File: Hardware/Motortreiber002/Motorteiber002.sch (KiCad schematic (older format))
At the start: 0 parts

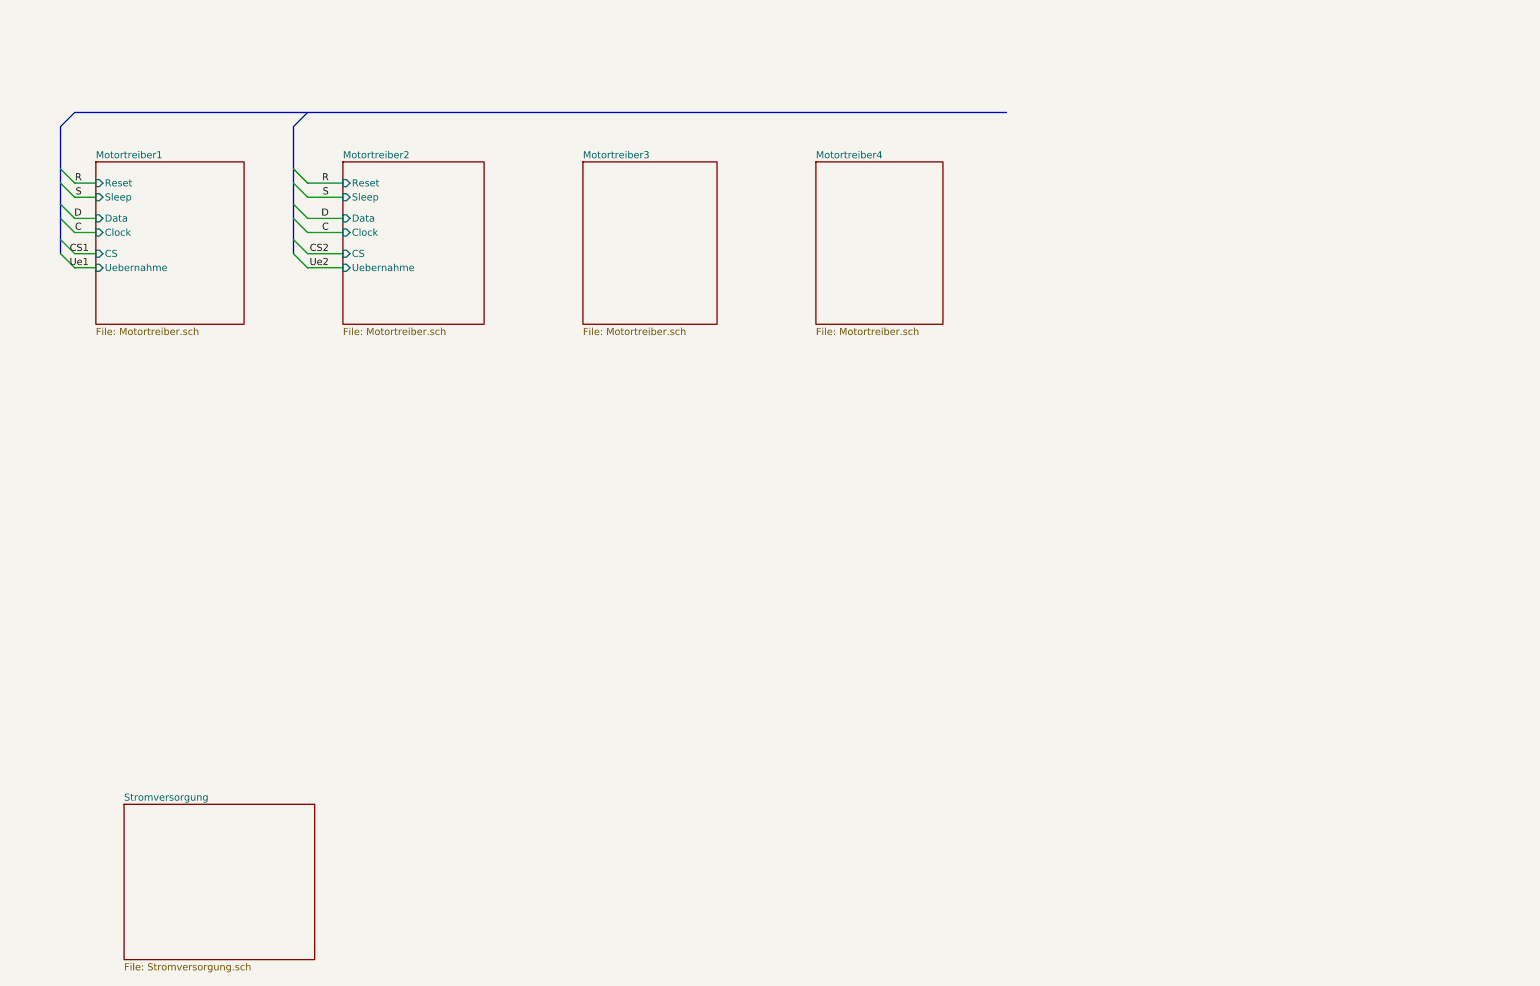
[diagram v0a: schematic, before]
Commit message: Mega64 hinzu
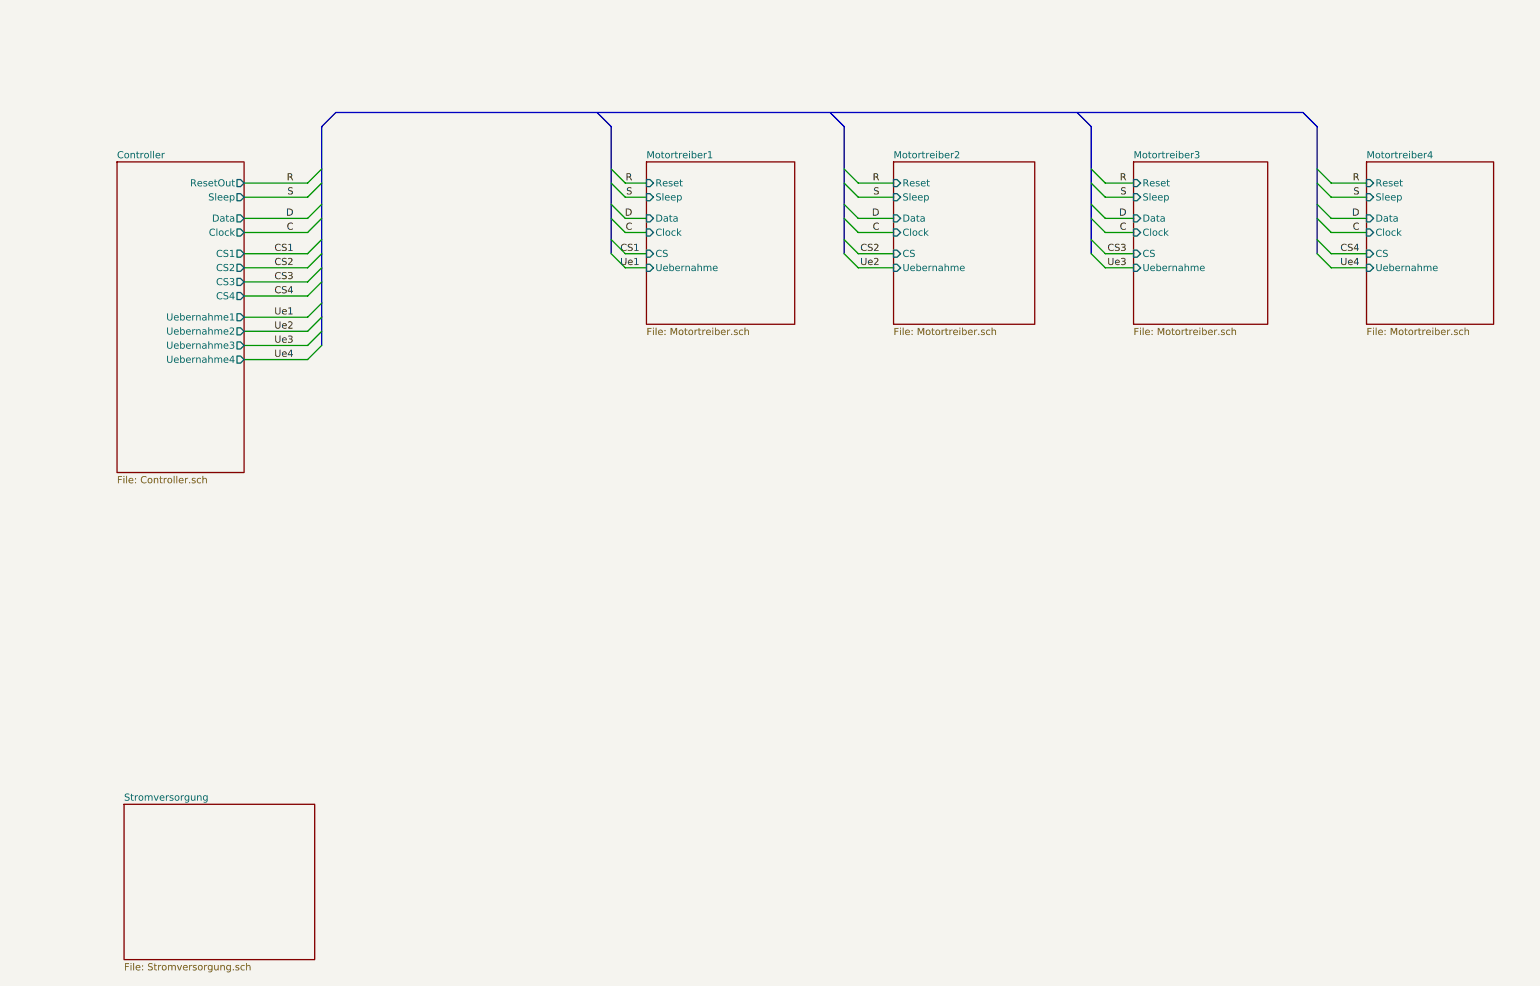
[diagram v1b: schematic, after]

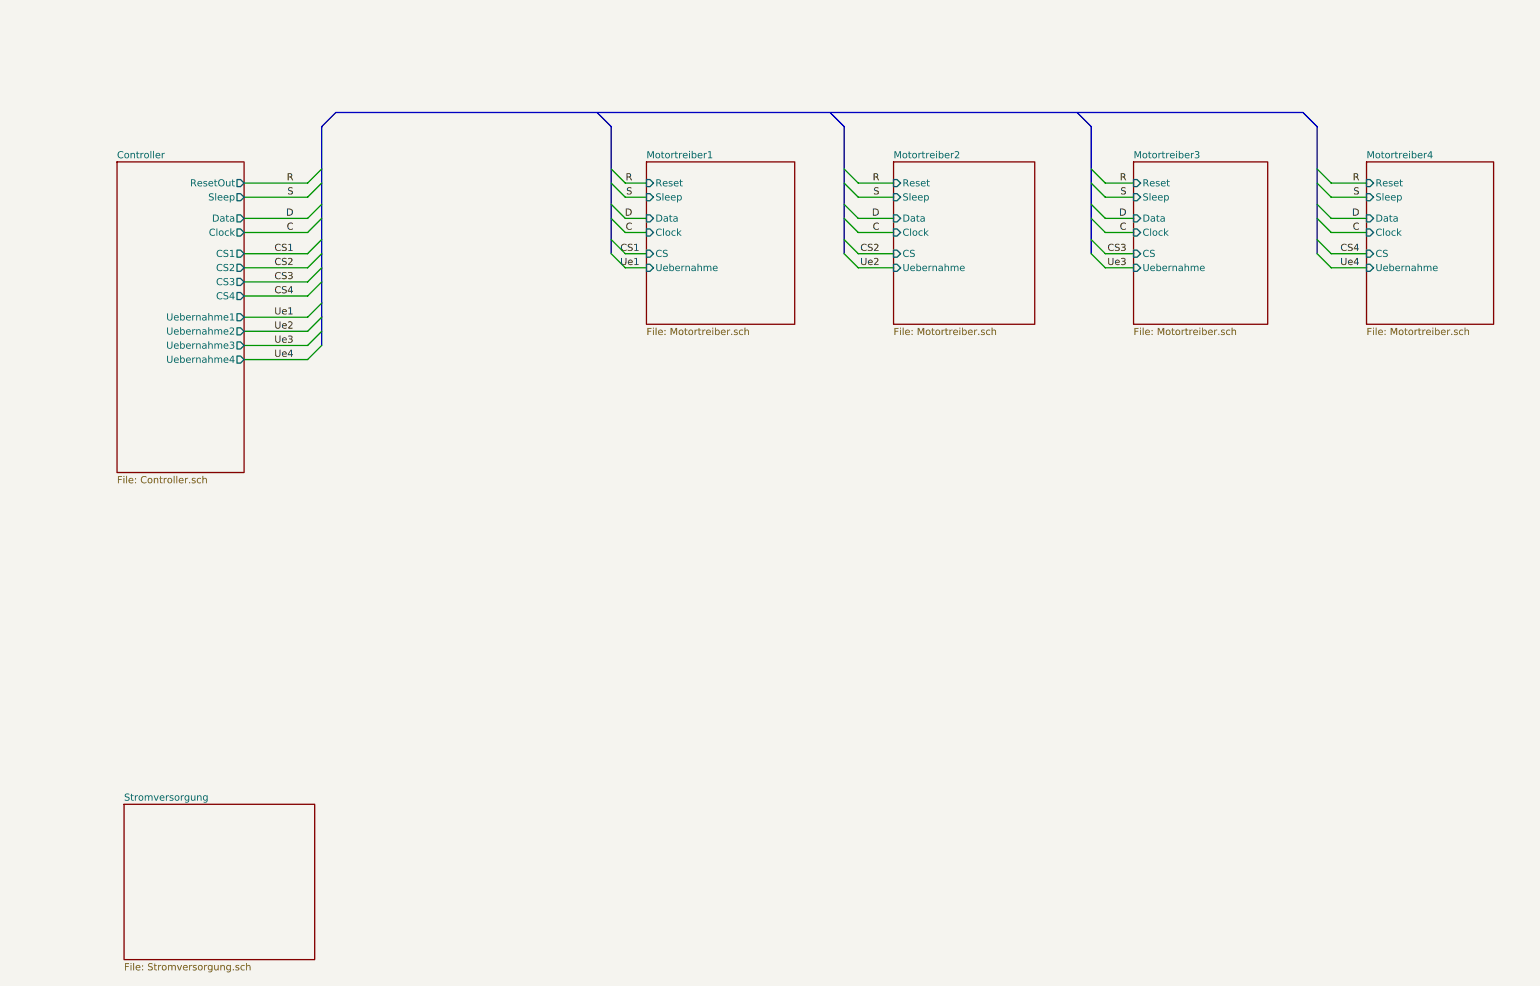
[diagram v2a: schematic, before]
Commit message: 16 Motortreiber 1 ATXMega 128 mit USB USB Anschluss noch nicht fertig
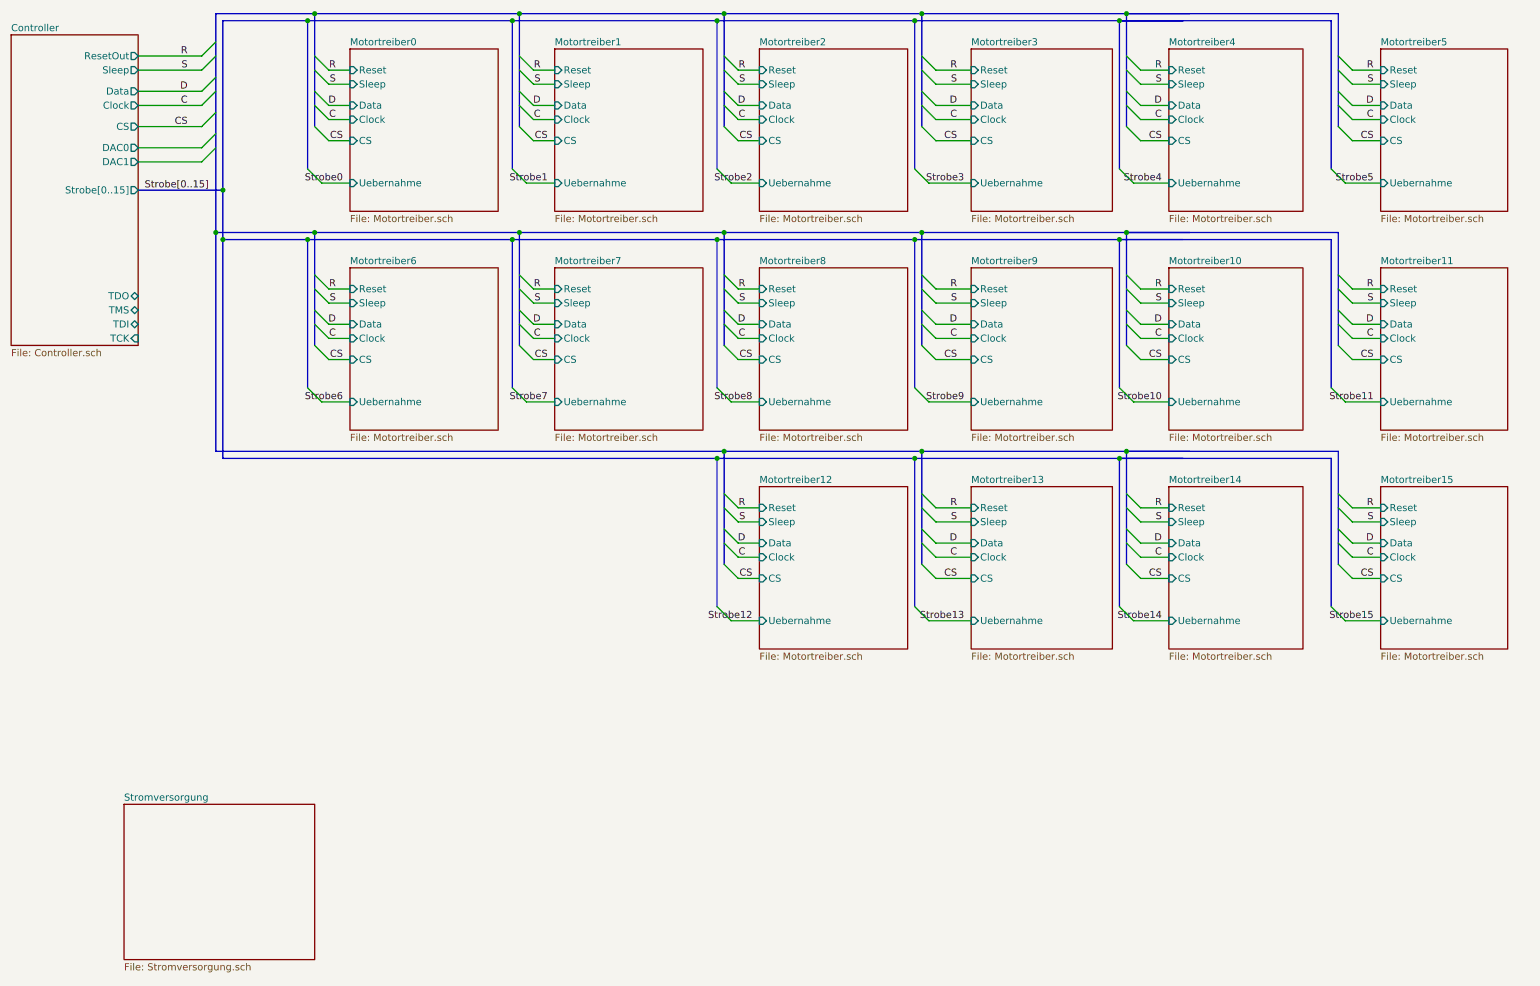
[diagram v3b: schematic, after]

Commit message: Annotation auf Seiten bezogen
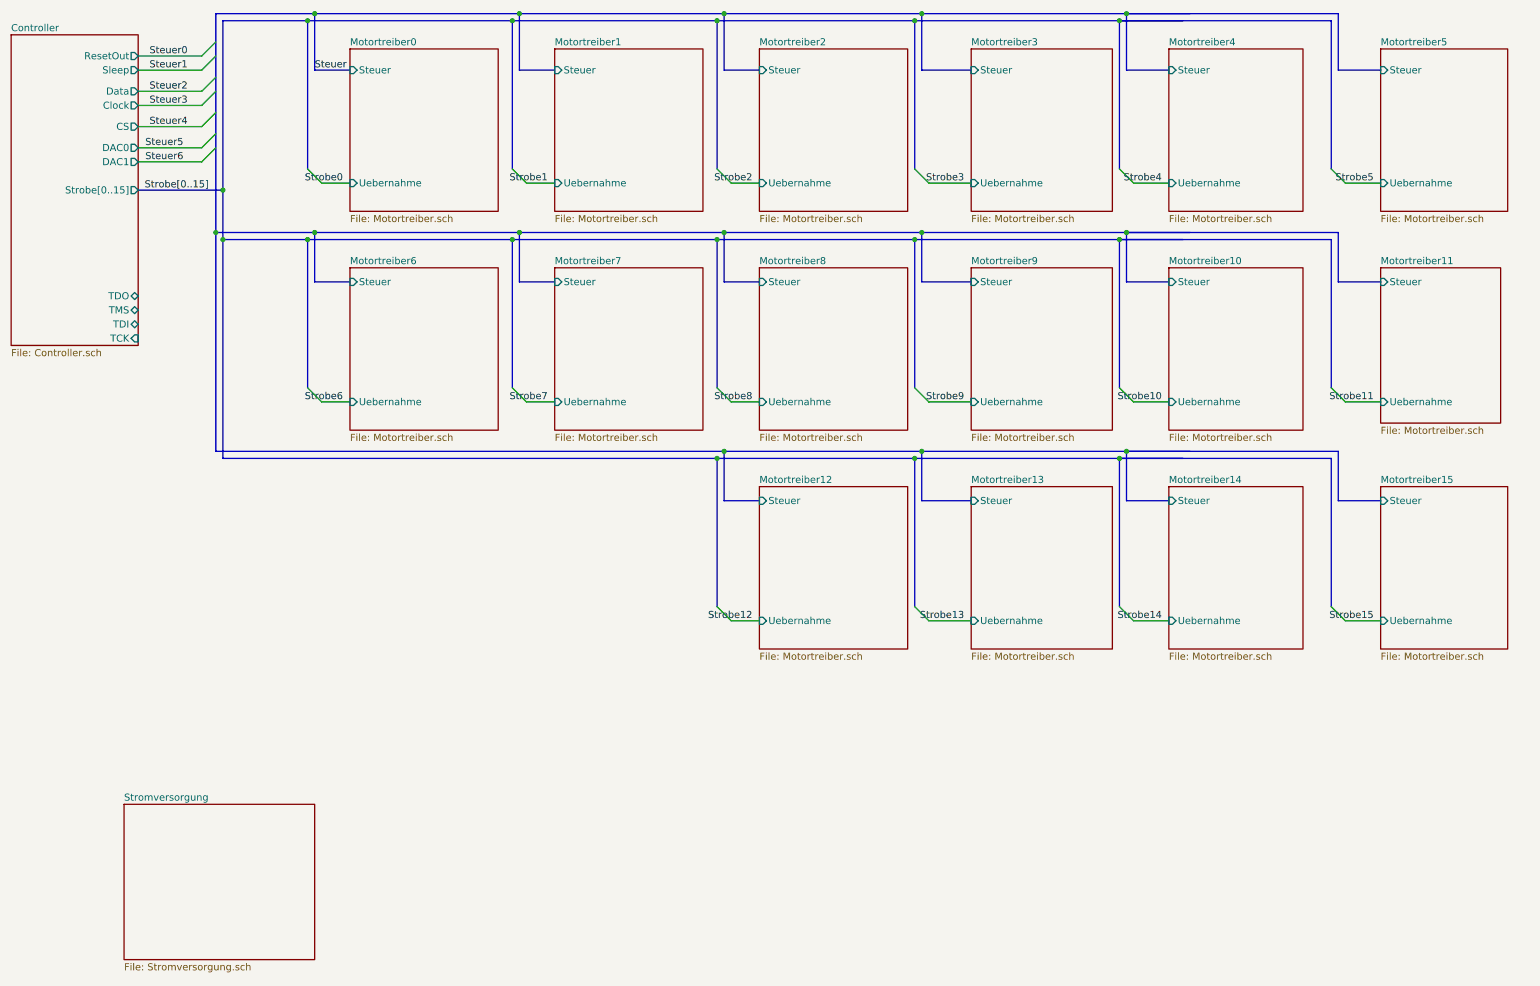
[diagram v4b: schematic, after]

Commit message: 16 Motortreiber
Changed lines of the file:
@@
 F1 "Motortreiber.sch" 50
 F2 "Uebernahme" I L 10300 1700 50
-F3 "Steuer" I L 10300 900 50
+F3 "Steuer[0..6]" I L 10300 900 50
 $EndSheet
 $Sheet
@@
 F1 "Motortreiber.sch" 50
 F2 "Uebernahme" I L 7400 1700 50
-F3 "Steuer" I L 7400 900 50
+F3 "Steuer[0..6]" I L 7400 900 50
 $EndSheet
 $Sheet
@@
 F1 "Motortreiber.sch" 50
 F2 "Uebernahme" I L 4450 1700 50
-F3 "Steuer" I L 4450 900 50
+F3 "Steuer[0..6]" I L 4450 900 50
 $EndSheet
 Wire Bus Line
@@
 F1 "Motortreiber.sch" 50
 F2 "Uebernahme" I L 3000 1700 50
-F3 "Steuer" I L 3000 900 50
+F3 "Steuer[0..6]" I L 3000 900 50
 $EndSheet
 Wire Bus Line
@@
 F1 "Motortreiber.sch" 50
 F2 "Uebernahme" I L 7400 3250 50
-F3 "Steuer" I L 7400 2400 50
+F3 "Steuer[0..6]" I L 7400 2400 50
 $EndSheet
 Wire Bus Line
@@
 F1 "Motortreiber.sch" 50
 F2 "Uebernahme" I L 3000 3250 50
-F3 "Steuer" I L 3000 2400 50
+F3 "Steuer[0..6]" I L 3000 2400 50
 $EndSheet
 Wire Bus Line
@@
 F1 "Motortreiber.sch" 50
 F2 "Uebernahme" I L 8800 4800 50
-F3 "Steuer" I L 8800 3950 50
+F3 "Steuer[0..6]" I L 8800 3950 50
 $EndSheet
 $Sheet
@@
 F1 "Motortreiber.sch" 50
 F2 "Uebernahme" I L 7400 4800 50
-F3 "Steuer" I L 7400 3950 50
+F3 "Steuer[0..6]" I L 7400 3950 50
 $EndSheet
 $Sheet
@@
 F1 "Motortreiber.sch" 50
 F2 "Uebernahme" I L 5900 4800 50
-F3 "Steuer" I L 5900 3950 50
+F3 "Steuer[0..6]" I L 5900 3950 50
 $EndSheet
 Wire Bus Line
@@
 	4200 500  4200 900
 Text Label 2750 900  0    50   ~ 0
-Steuer
+Steuer[0..6]
 Wire Bus Line
 	5650 500  5650 900
@@
 F1 "Motortreiber.sch" 50
 F2 "Uebernahme" I L 5900 1700 50
-F3 "Steuer" I L 5900 900 50
+F3 "Steuer[0..6]" I L 5900 900 50
 $EndSheet
 Wire Bus Line
@@
 F1 "Motortreiber.sch" 50
 F2 "Uebernahme" I L 4450 3250 50
-F3 "Steuer" I L 4450 2400 50
+F3 "Steuer[0..6]" I L 4450 2400 50
 $EndSheet
 Wire Bus Line
@@
 F1 "Motortreiber.sch" 50
 F2 "Uebernahme" I L 5900 3250 50
-F3 "Steuer" I L 5900 2400 50
+F3 "Steuer[0..6]" I L 5900 2400 50
 $EndSheet
 Wire Bus Line
@@
 F1 "Motortreiber.sch" 50
 F2 "Uebernahme" I L 8800 1700 50
-F3 "Steuer" I L 8800 900 50
+F3 "Steuer[0..6]" I L 8800 900 50
 $EndSheet
 Wire Bus Line
@@
 F1 "Motortreiber.sch" 50
 F2 "Uebernahme" I L 8800 3250 50
-F3 "Steuer" I L 8800 2400 50
+F3 "Steuer[0..6]" I L 8800 2400 50
 $EndSheet
 Wire Bus Line
@@
 F1 "Motortreiber.sch" 50
 F2 "Uebernahme" I L 10300 4800 50
-F3 "Steuer" I L 10300 3950 50
+F3 "Steuer[0..6]" I L 10300 3950 50
 $EndSheet
 Wire Bus Line
@@
 F0 "Motortreiber11" 50
 F1 "Motortreiber.sch" 50
-F2 "Steuer" I L 10300 2400 50
-F3 "Uebernahme" I L 10300 3250 50
-$EndSheet
-Wire Bus Line
+F2 "Uebernahme" I L 10300 3250 50
+F3 "Steuer[0..6]" I L 10300 2400 50
+$EndSheet
+Wire Bus Line
